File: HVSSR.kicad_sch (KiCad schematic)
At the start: 2 parts, among them U8 AQH2223A

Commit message: update some footprints etc
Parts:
- renumbered R6 to R12
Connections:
- net EN (3V3): now also U8.2; no longer R12.1
- net GND: now also R12.1; no longer U8.1, U8.3, U8.4
- net at R12.2: now also U8.1, U8.3, U8.4; no longer U8.2
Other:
- moved on the sheet: R12
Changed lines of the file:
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@@
 	(wire
 		(pts
-			(xy 107.95 82.55) (xy 114.3 82.55)
+			(xy 107.95 82.55) (xy 127 82.55)
 		)
 		(stroke
@@
 	(wire
 		(pts
+			(xy 123.19 90.17) (xy 127 90.17)
+		)
+		(stroke
+			(width 0)
+			(type default)
+		)
+	)
+	(wire
+		(pts
 			(xy 144.78 82.55) (xy 147.32 82.55)
 		)
@@
 	(wire
 		(pts
-			(xy 121.92 82.55) (xy 127 82.55)
-		)
-		(stroke
-			(width 0)
-			(type default)
-		)
-	)
-	(wire
-		(pts
-			(xy 107.95 90.17) (xy 127 90.17)
+			(xy 107.95 90.17) (xy 115.57 90.17)
 		)
 		(stroke
@@
 	(symbol
 		(lib_id "Device:R")
-		(at 118.11 82.55 90)
+		(at 119.38 90.17 90)
 		(unit 1)
 		(exclude_from_sim no)
@@
 		(dnp no)
 		(fields_autoplaced yes)
-		(property "Reference" "R6"
-			(at 118.11 76.2 90)
+		(property "Reference" "R12"
+			(at 119.38 83.82 90)
 			(effects
 				(font
@@
 		)
 		(property "Value" "150"
-			(at 118.11 78.74 90)
+			(at 119.38 86.36 90)
 			(effects
 				(font
@@
 		)
 		(property "Footprint" "Resistor_SMD:R_0201_0603Metric"
-			(at 118.11 84.328 90)
+			(at 119.38 91.948 90)
 			(effects
 				(font
@@
 		)
 		(property "Datasheet" "~"
-			(at 118.11 82.55 0)
+			(at 119.38 90.17 0)
 			(effects
 				(font
@@
 		)
 		(property "Description" "Resistor"
-			(at 118.11 82.55 0)
+			(at 119.38 90.17 0)
 			(effects
 				(font
@@
 			(project "GaggiMate"
 				(path "/18f69721-6a2b-4a2b-8e72-291680dbbe9a/408458ba-3d65-4408-a5a0-5df4ee162e36"
+					(reference "R12")
+					(unit 1)
+				)
+				(path "/18f69721-6a2b-4a2b-8e72-291680dbbe9a/f7f28c5c-b8c9-48cd-824f-13eab97dd33b"
 					(reference "R6")
 					(unit 1)
 				)
-				(path "/18f69721-6a2b-4a2b-8e72-291680dbbe9a/f7f28c5c-b8c9-48cd-824f-13eab97dd33b"
-					(reference "R7")
-					(unit 1)
-				)

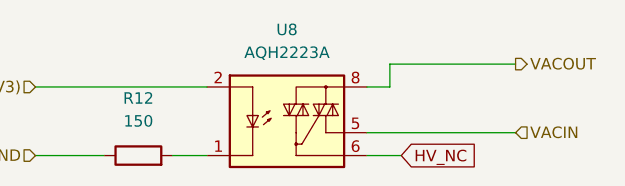
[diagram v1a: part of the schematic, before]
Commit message: Moved front side components to other board, finished cap and resistor selection and maybe finalizing layout
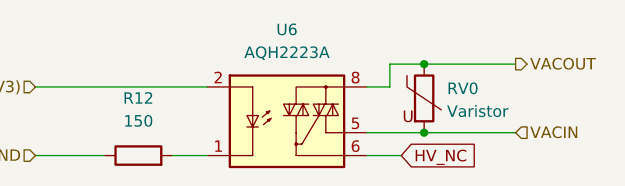
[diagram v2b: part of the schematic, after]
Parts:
- added RV0: Varistor, Diode_SMD:D_1210_3225Metric, symbol Device:Varistor
- R12: footprint Resistor_SMD:R_0201_0603Metric -> Resistor_SMD:R_0603_1608Metric
- renumbered U8 to U6
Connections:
- net VACIN: now also RV0.2
- net VACOUT: now also RV0.1
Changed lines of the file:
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@@
 	(generator_version "9.0")
 	(paper "A4")
+	(junction
+		(at 151.13 87.63)
+		(diameter 0)
+		(color 0 0 0 0)
+	)
+	(junction
+		(at 151.13 80.01)
+		(diameter 0)
+		(color 0 0 0 0)
+	)
+	(wire
+		(pts
+			(xy 151.13 87.63) (xy 161.29 87.63)
+		)
+		(stroke
+			(width 0)
+			(type default)
+		)
+	)
 	(wire
 		(pts
@@
 	(wire
 		(pts
-			(xy 144.78 87.63) (xy 161.29 87.63)
+			(xy 144.78 87.63) (xy 151.13 87.63)
 		)
 		(stroke
@@
 	(wire
 		(pts
-			(xy 147.32 80.01) (xy 161.29 80.01)
+			(xy 151.13 80.01) (xy 161.29 80.01)
+		)
+		(stroke
+			(width 0)
+			(type default)
+		)
+	)
+	(wire
+		(pts
+			(xy 147.32 80.01) (xy 151.13 80.01)
 		)
 		(stroke
@@
 			)
 			(justify left)
+		)
+	)
+	(symbol
+		(lib_id "Device:Varistor")
+		(at 151.13 83.82 0)
+		(unit 1)
+		(exclude_from_sim no)
+		(in_bom yes)
+		(on_board yes)
+		(dnp no)
+		(fields_autoplaced yes)
+		(property "Reference" "RV0"
+			(at 153.67 82.7432 0)
+			(effects
+				(font
+					(size 1.27 1.27)
+				)
+				(justify left)
+			)
+		)
+		(property "Value" "Varistor"
+			(at 153.67 85.2832 0)
+			(effects
+				(font
+					(size 1.27 1.27)
+				)
+				(justify left)
+			)
+		)
+		(property "Footprint" "Diode_SMD:D_1210_3225Metric"
+			(at 149.352 83.82 90)
+			(effects
+				(font
+					(size 1.27 1.27)
+				)
+				(hide yes)
+			)
+		)
+		(property "Datasheet" "~"
+			(at 151.13 83.82 0)
+			(effects
+				(font
+					(size 1.27 1.27)
+				)
+				(hide yes)
+			)
+		)
+		(property "Description" "Voltage dependent resistor"
+			(at 151.13 83.82 0)
+			(effects
+				(font
+					(size 1.27 1.27)
+				)
+				(hide yes)
+			)
+		)
+		(property "Sim.Name" "kicad_builtin_varistor"
+			(at 151.13 83.82 0)
+			(effects
+				(font
+					(size 1.27 1.27)
+				)
+				(hide yes)
+			)
+		)
+		(property "Sim.Device" "SUBCKT"
+			(at 151.13 83.82 0)
+			(effects
+				(font
+					(size 1.27 1.27)
+				)
+				(hide yes)
+			)
+		)
+		(property "Sim.Pins" "1=A 2=B"
+			(at 151.13 83.82 0)
+			(effects
+				(font
+					(size 1.27 1.27)
+				)
+				(hide yes)
+			)
+		)
+		(property "Sim.Params" "threshold=1k"
+			(at 151.13 83.82 0)
+			(effects
+				(font
+					(size 1.27 1.27)
+				)
+				(hide yes)
+			)
+		)
+		(property "Sim.Library" "${KICAD9_SYMBOL_DIR}/Simulation_SPICE.sp"
+			(at 151.13 83.82 0)
+			(effects
+				(font
+					(size 1.27 1.27)
+				)
+				(hide yes)
+			)
+		)
+		(pin "2"
+		)
+		(pin "1"
+		)
+		(instances
+			(project ""
+				(path "/18f69721-6a2b-4a2b-8e72-291680dbbe9a/408458ba-3d65-4408-a5a0-5df4ee162e36"
+					(reference "RV0")
+					(unit 1)
+				)
+				(path "/18f69721-6a2b-4a2b-8e72-291680dbbe9a/f7f28c5c-b8c9-48cd-824f-13eab97dd33b"
+					(reference "RV1")
+					(unit 1)
+				)
+			)
 		)
 	)
@@
 			)
 		)
-		(property "Footprint" "Resistor_SMD:R_0201_0603Metric"
+		(property "Footprint" "Resistor_SMD:R_0603_1608Metric"
 			(at 119.38 91.948 90)
 			(effects
@@
 				)
 				(path "/18f69721-6a2b-4a2b-8e72-291680dbbe9a/f7f28c5c-b8c9-48cd-824f-13eab97dd33b"
-					(reference "R6")
+					(reference "R7")
 					(unit 1)
 				)
@@
 		(dnp no)
 		(fields_autoplaced yes)
-		(property "Reference" "U8"
+		(property "Reference" "U6"
 			(at 135.89 76.2 0)
 			(effects
@@
 			(project ""
 				(path "/18f69721-6a2b-4a2b-8e72-291680dbbe9a/408458ba-3d65-4408-a5a0-5df4ee162e36"
-					(reference "U8")
+					(reference "U6")
 					(unit 1)
 				)
 				(path "/18f69721-6a2b-4a2b-8e72-291680dbbe9a/f7f28c5c-b8c9-48cd-824f-13eab97dd33b"
-					(reference "U9")
-					(unit 1)
-				)
+					(reference "U3")
+					(unit 1)
+				)

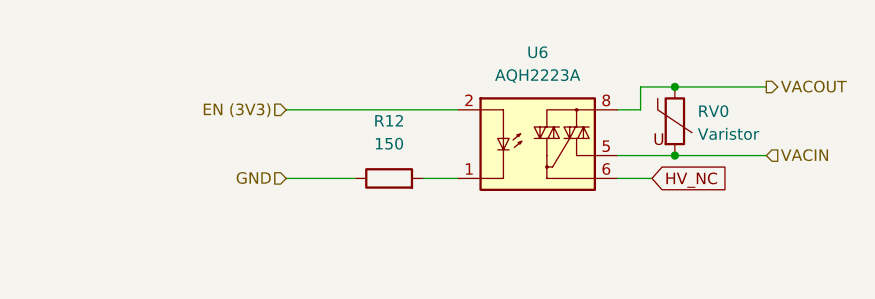
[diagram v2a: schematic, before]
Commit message: geographical referencing instead
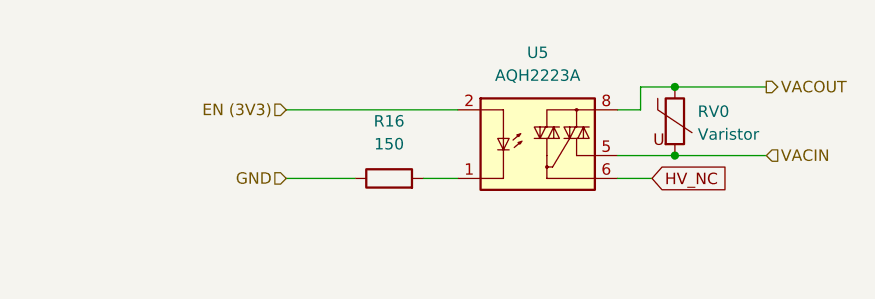
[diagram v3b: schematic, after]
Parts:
- renumbered R12 to R16, U6 to U5
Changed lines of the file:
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@@
 		(dnp no)
 		(fields_autoplaced yes)
-		(property "Reference" "R12"
+		(property "Reference" "R16"
 			(at 119.38 83.82 90)
 			(effects
@@
 			(project "GaggiMate"
 				(path "/18f69721-6a2b-4a2b-8e72-291680dbbe9a/408458ba-3d65-4408-a5a0-5df4ee162e36"
-					(reference "R12")
+					(reference "R16")
 					(unit 1)
 				)
@@
 		(dnp no)
 		(fields_autoplaced yes)
-		(property "Reference" "U6"
+		(property "Reference" "U5"
 			(at 135.89 76.2 0)
 			(effects
@@
 			(project ""
 				(path "/18f69721-6a2b-4a2b-8e72-291680dbbe9a/408458ba-3d65-4408-a5a0-5df4ee162e36"
-					(reference "U6")
+					(reference "U5")
 					(unit 1)
 				)

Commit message: attempt some routing
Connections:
- net HV_NC: no longer names the net of U5.6
- no-connect marks 0 -> 1
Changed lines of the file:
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@@
 		(color 0 0 0 0)
+	)
+	(no_connect
+		(at 144.78 90.17)
 	)
 	(wire
@@
 		)
 	)
-	(wire
-		(pts
-			(xy 148.59 90.17) (xy 144.78 90.17)
-		)
-		(stroke
-			(width 0)
-			(type default)
-		)
-	)
-	(global_label "HV_NC"
-		(shape input)
-		(at 148.59 90.17 0)
-		(fields_autoplaced yes)
-		(effects
-			(font
-				(size 1.27 1.27)
-			)
-			(justify left)
-		)
-		(property "Intersheetrefs" "${INTERSHEET_REFS}"
-			(at 157.5624 90.17 0)
-			(effects
-				(font
-					(size 1.27 1.27)
-				)
-				(justify left)
-				(hide yes)
-			)
-		)
-	)

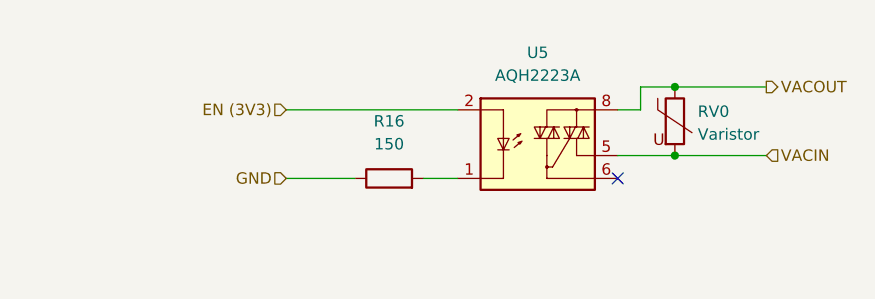
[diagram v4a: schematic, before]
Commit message: add custom silkscreen and missing lilygo out pins
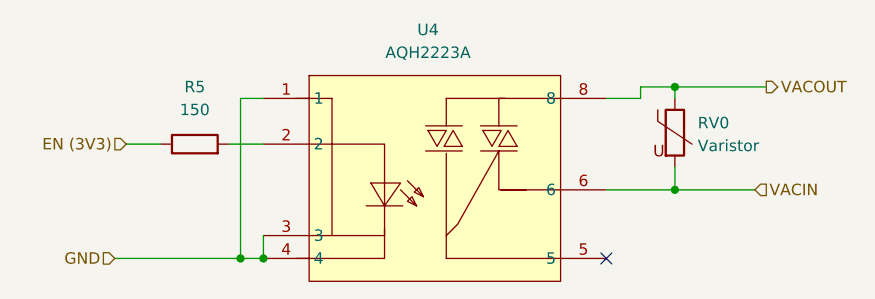
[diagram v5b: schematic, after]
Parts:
- removed U5: AQH2223A, Package_SO:SSO-7-8_6.4x9.78mm_P2.54mm, symbol Relay_SolidState:AQH2223A
- added U4: AQH2223A, easyeda2kicad:SMD-8_7P-L9.8-W6.4-P2.54-BL-PE7, symbol easyeda2kicad:AQH2223A
- RV0: footprint Diode_SMD:D_1210_3225Metric -> easyeda2kicad:RES-SMD_L6.8-W5.9-LS7.8
- renumbered R16 to R5
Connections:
- net EN (3V3): now also R5.1
- net GND: now also U4.1, U4.3, U4.4; no longer R5.1
- net VACIN: now also U4.6
- net VACOUT: now also U4.8
- net at R5.2: now also U4.2
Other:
- moved on the sheet: R5, RV0
